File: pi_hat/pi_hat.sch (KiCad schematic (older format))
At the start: 42 parts, among them J1 Conn_Coaxial, J2 Conn_Coaxial, J3 Conn_02x20_Odd_Even, J4 Conn_02x04_Odd_Even, J5 Conn_02x02_Odd_Even, T1 2873002402, T2 2873002402, U1 FOX924, U2 Si5351A-B-GM, U3 FST3253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

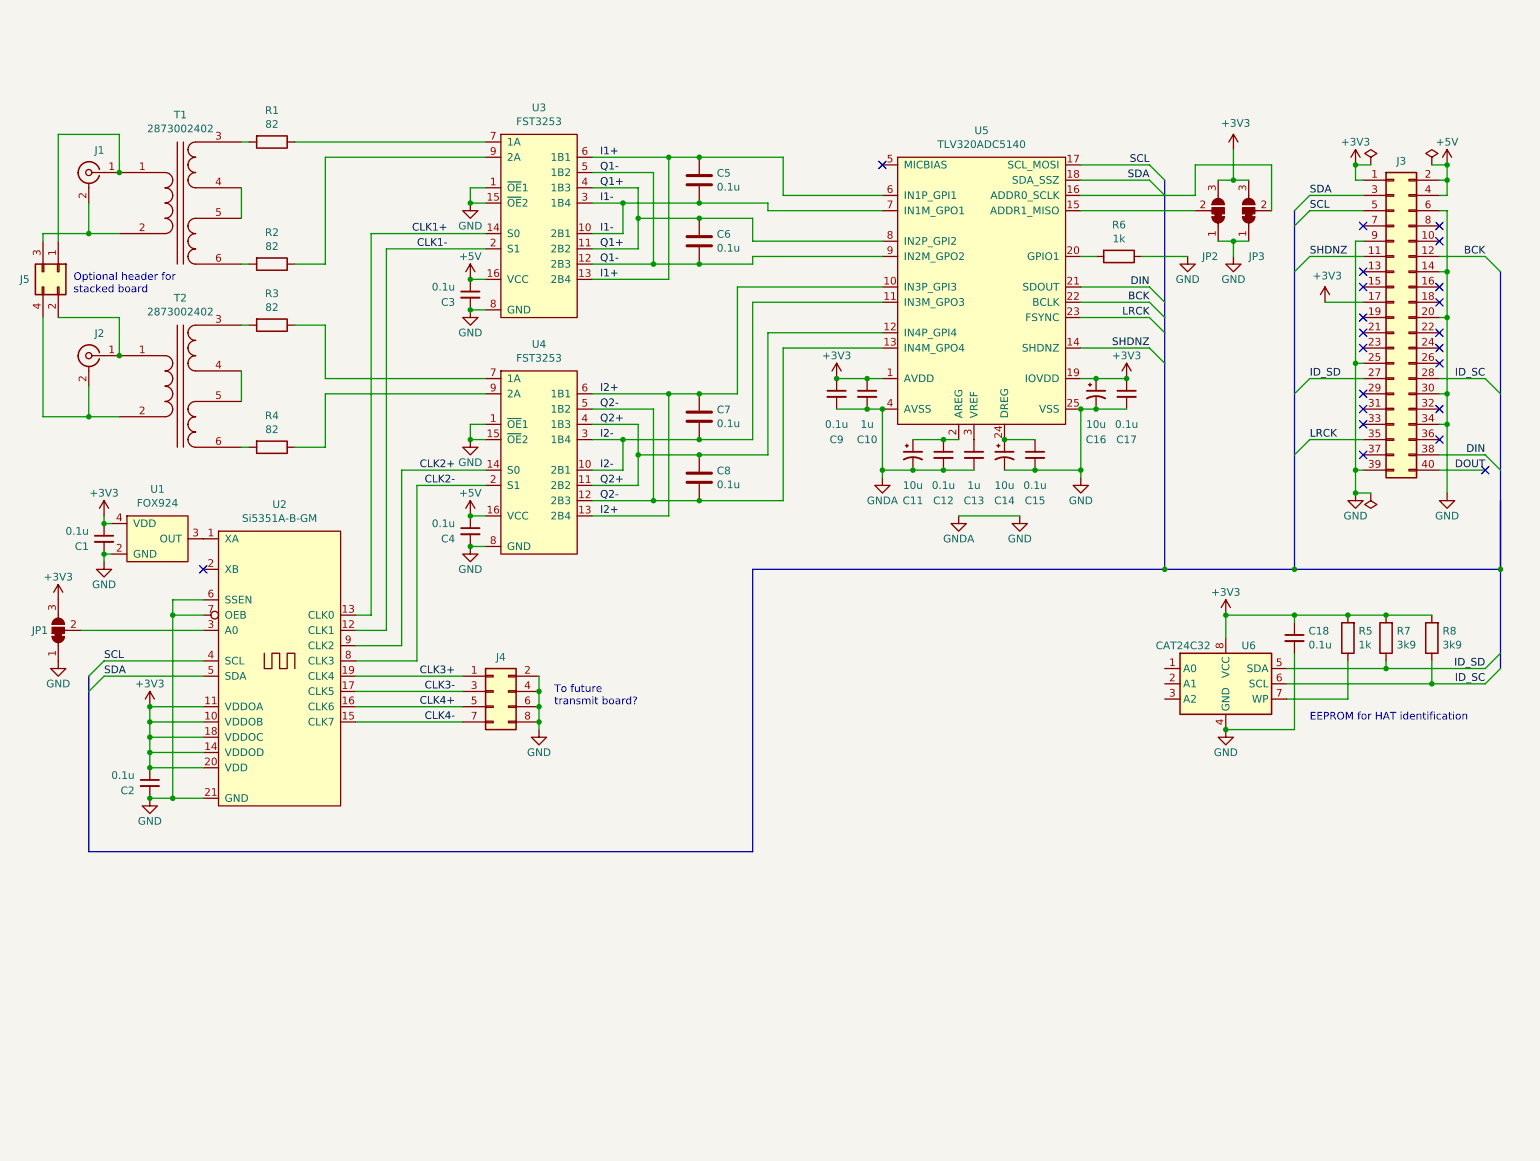
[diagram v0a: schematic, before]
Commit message: Add header for external filter board
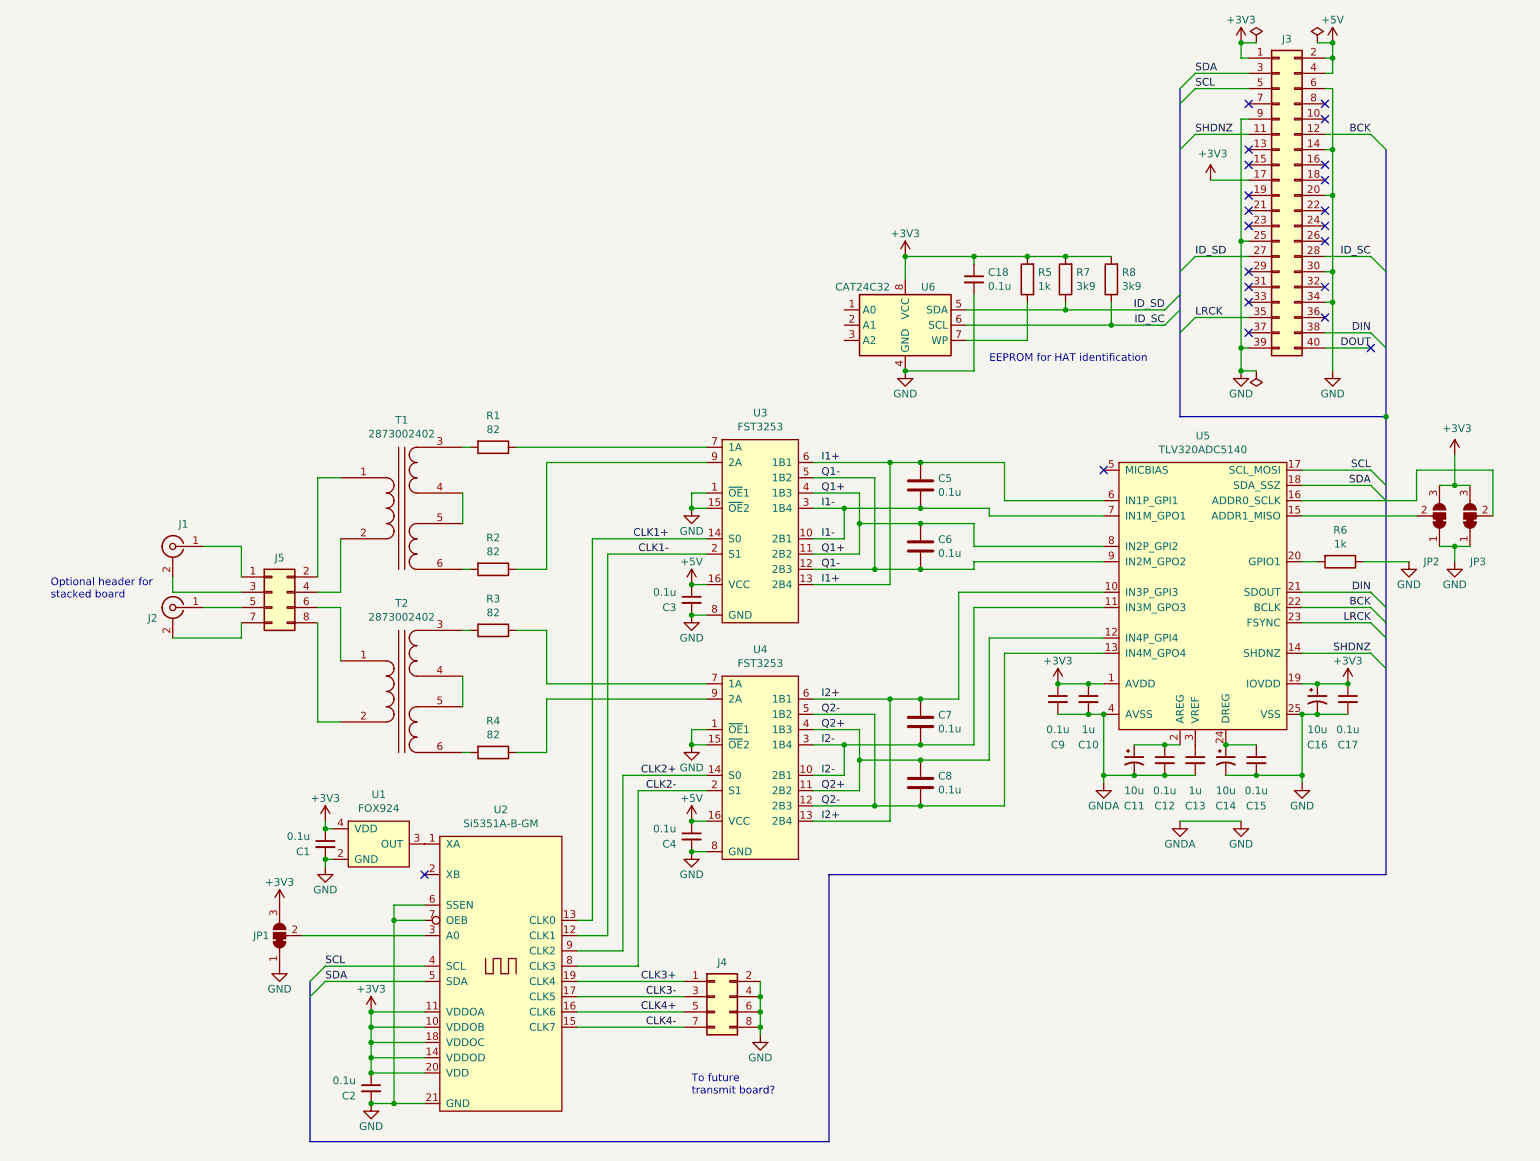
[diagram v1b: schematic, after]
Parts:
- removed J5: Conn_02x02_Odd_Even, Connector_PinHeader_2.54mm:PinHeader_2x02_P2.54mm_Vertical, symbol Connector_Generic:Conn_02x02_Odd_Even
- added J5: Conn_02x04_Odd_Even, Connector_PinHeader_2.54mm:PinHeader_2x04_P2.54mm_Vertical, symbol Connector_Generic:Conn_02x04_Odd_Even
- J3: footprint Connector_PinHeader_2.54mm:PinHeader_2x20_P2.54mm_Vertical -> Bitglue:Pi_HAT
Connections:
- net at T2.1 (AA): now also J5.6 (Pin_6); no longer J2.1 (In)
- net at T2.2 (AB): now also J5.8 (Pin_8); no longer J2.2 (Ext)
- net at J1.1 (In): now also J5.1 (Pin_1); no longer T1.1 (AA)
- net at J1.2 (Ext): now also J5.3 (Pin_3); no longer T1.2 (AB)
- new net: J2.1 (In), J5.5 (Pin_5)
- new net: J2.2 (Ext), J5.7 (Pin_7)
- new net: J5.2 (Pin_2), T1.1 (AA)
- new net: J5.4 (Pin_4), T1.2 (AB)
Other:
- moved on the sheet: C1, C10, C11, C12, C13, C14, C15, C16, C17, C18, C2, C3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

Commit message: Add additional decoupling capacitors
Si5351 datasheet says we need one per supply pin.

Also added a couple caps right at the Pi header. Seemed like a good idea
to limit noise coming on to the board.
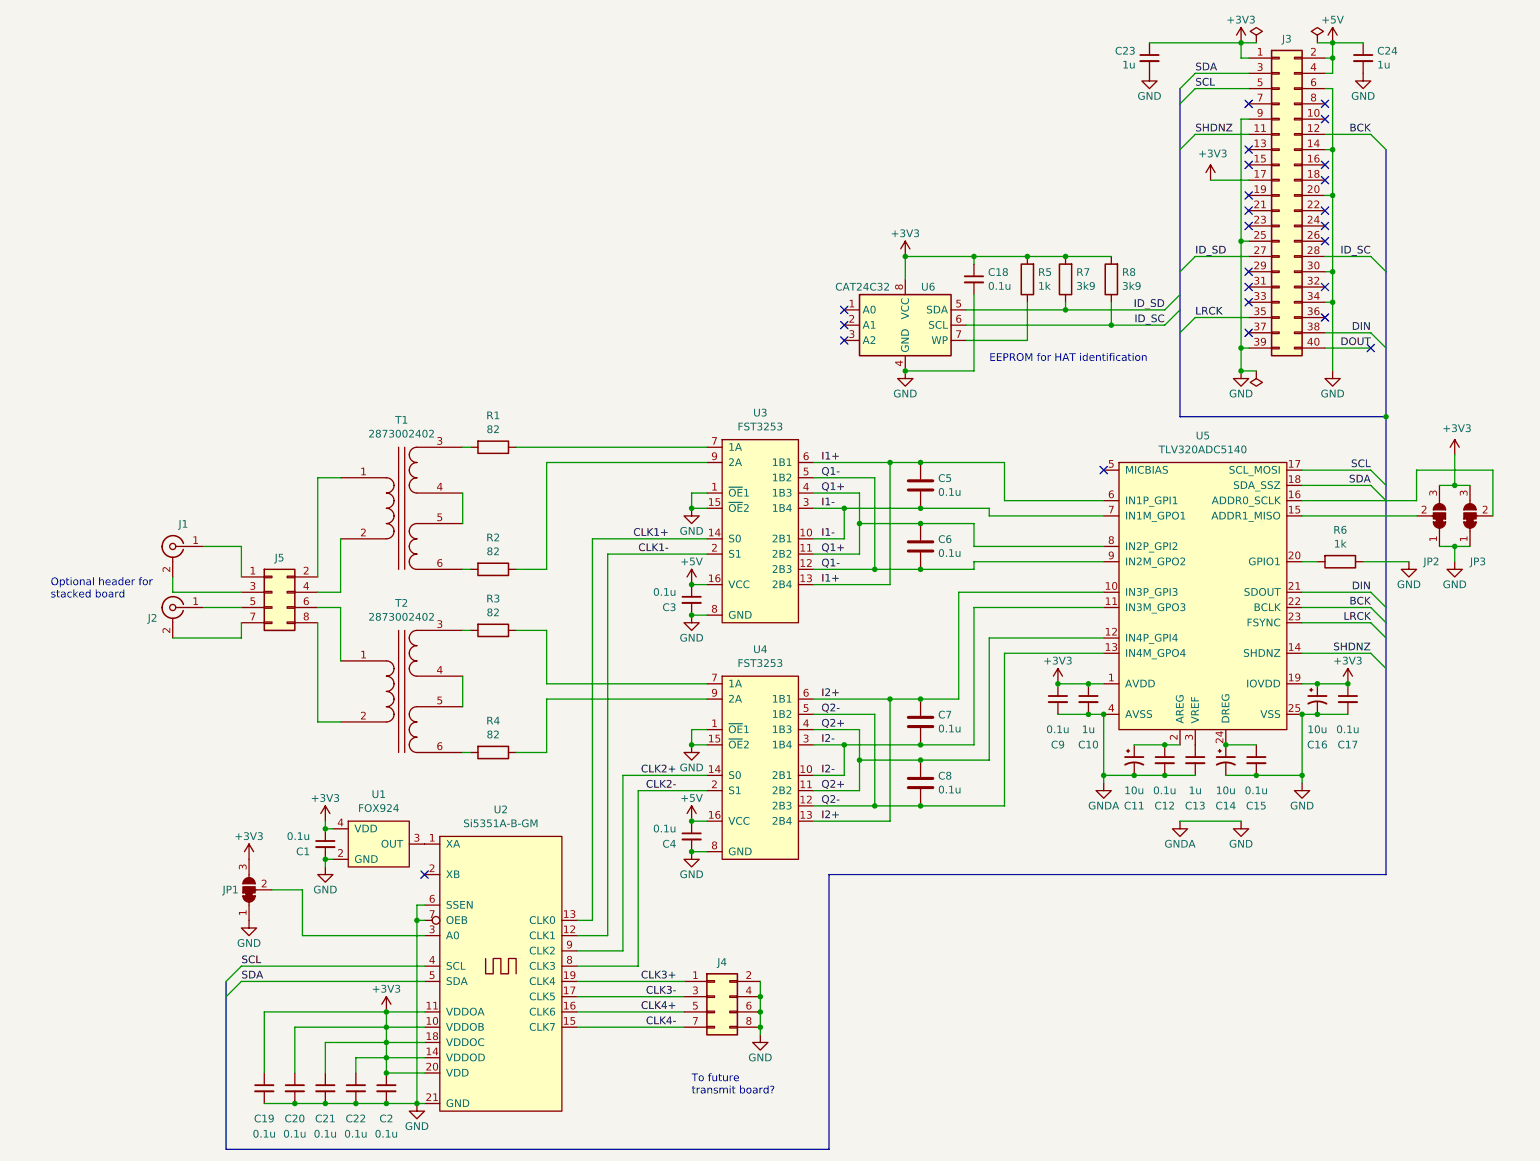
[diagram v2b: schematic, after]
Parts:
- added C19, C20, C21, C22: 0.1u, Capacitor_SMD:C_1206_3216Metric_Pad1.42x1.75mm_HandSolder, symbol Device:C_Small
- added C23, C24: 1u, Capacitor_SMD:C_1206_3216Metric_Pad1.42x1.75mm_HandSolder, symbol Device:C_Small
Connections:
- net +3V3: now also C19.1, C20.1, C21.1, C22.1, C23.1
- net +5V: now also C24.1
- net GND: now also C19.2, C20.2, C21.2, C22.2, C23.2, C24.2
- no-connect marks 22 -> 25
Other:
- moved on the sheet: C2, JP1

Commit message: Improve layout after review
- Move I2C lines from under decoupling cap
- Beef up power supply traces and add more vias
- Add another 3.3V bypass cap near the header

Also, added a .100" grid of plated holes in the unused area, because why
not.
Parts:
- added C25: 1u, Capacitor_SMD:C_1206_3216Metric_Pad1.42x1.75mm_HandSolder, symbol Device:C_Small
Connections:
- net +3V3: now also C25.1
- net GND: now also C25.2
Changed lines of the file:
@@
 U 1 1 5F0CEBCD
 P 7950 850
-F 0 "C23" H 7859 896 50  0000 R CNN
-F 1 "1u" H 7859 805 50  0000 R CNN
+F 0 "C23" H 8042 896 50  0000 L CNN
+F 1 "1u" H 8042 805 50  0000 L CNN
 F 2 "Capacitor_SMD:C_1206_3216Metric_Pad1.42x1.75mm_HandSolder" H 7950 850 50  0001 C CNN
 F 3 "~" H 7950 850 50  0001 C CNN
@@
 Wire Wire Line
 	9150 750  9350 750
+$Comp
+L Device:C_Small C25
+U 1 1 5EBEFF50
+P 7750 850
+F 0 "C25" H 7659 896 50  0000 R CNN
+F 1 "1u" H 7659 805 50  0000 R CNN
+F 2 "Capacitor_SMD:C_1206_3216Metric_Pad1.42x1.75mm_HandSolder" H 7750 850 50  0001 C CNN
+F 3 "~" H 7750 850 50  0001 C CNN
+	1    7750 850
+	1    0    0    -1
+$EndComp
+Wire Wire Line
+	7950 750  7750 750
+Connection ~ 7950 750
+Wire Wire Line
+	7750 950  7950 950
 Wire Wire Line
 	8950 3750 9700 3750
@@
 Wire Bus Line
 	8150 1050 8150 3200
+Connection ~ 7950 950
 $EndSCHEMATC

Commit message: Add manufacturer part numbers to schematic
This works well with KiCost to generate a BOM.
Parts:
- C1, C12, C15, C17, C18, C19, C2, C20, C21, C22, C3, C4, C5, C6, C7, C8, C9: mpn (none) -> C1206C104M5RAC
- C10, C13, C23, C24, C25: mpn (none) -> C1206C105M3RACTU
- C11, C14, C16: mpn (none) -> C1206C106M3PAC
- J1, J2: mpn (none) -> CON-SMA-EDGE-S
- J3: mpn (none) -> SSQ-120-03-T-D
- JP1, JP2, JP3: DNP (none) -> 1
- R1, R2, R3, R4: mpn (none) -> CR1206-FX-82R0ELF
- R5, R6: mpn (none) -> CRCW12061K00FKEBC
- R7, R8: mpn (none) -> CRCW12063K90FKEAC
- T1, T2: mpn (none) -> 2873002402
- U1: mpn (none) -> FT5HNBPK27.0-T1
- U2: mpn (none) -> SI5351A-B-GM
- U3, U4: mpn (none) -> FST3253MTCX
- U5: mpn (none) -> TLV320ADC5140IRTWR
- U6: mpn (none) -> CAT24C32WI-GT3
